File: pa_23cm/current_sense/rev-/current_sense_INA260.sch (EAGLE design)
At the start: 34 parts, among them IC1 INA260, IC2 MCP9700

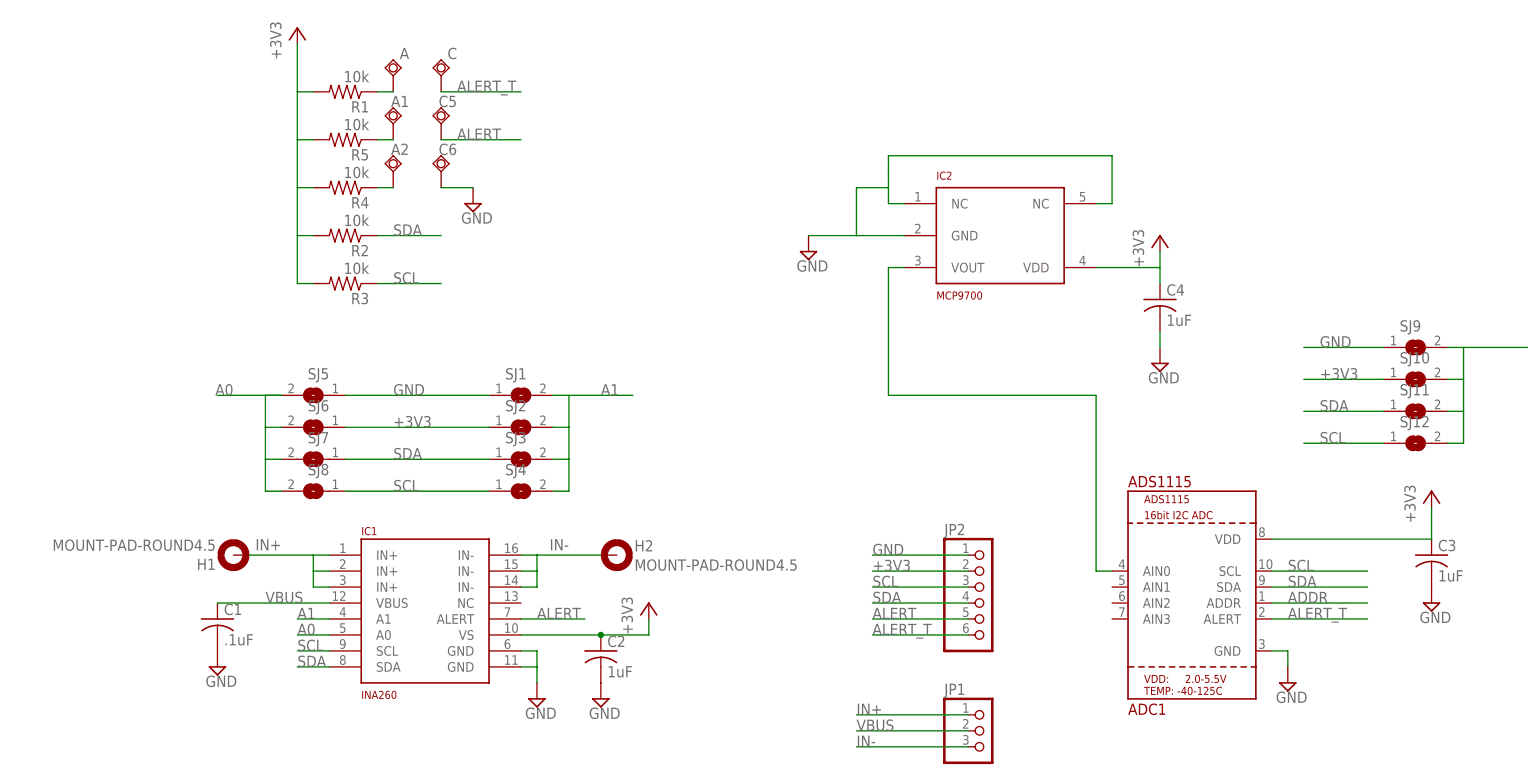
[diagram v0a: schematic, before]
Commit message: added Analog Input breakout for ADS1115 ADC.
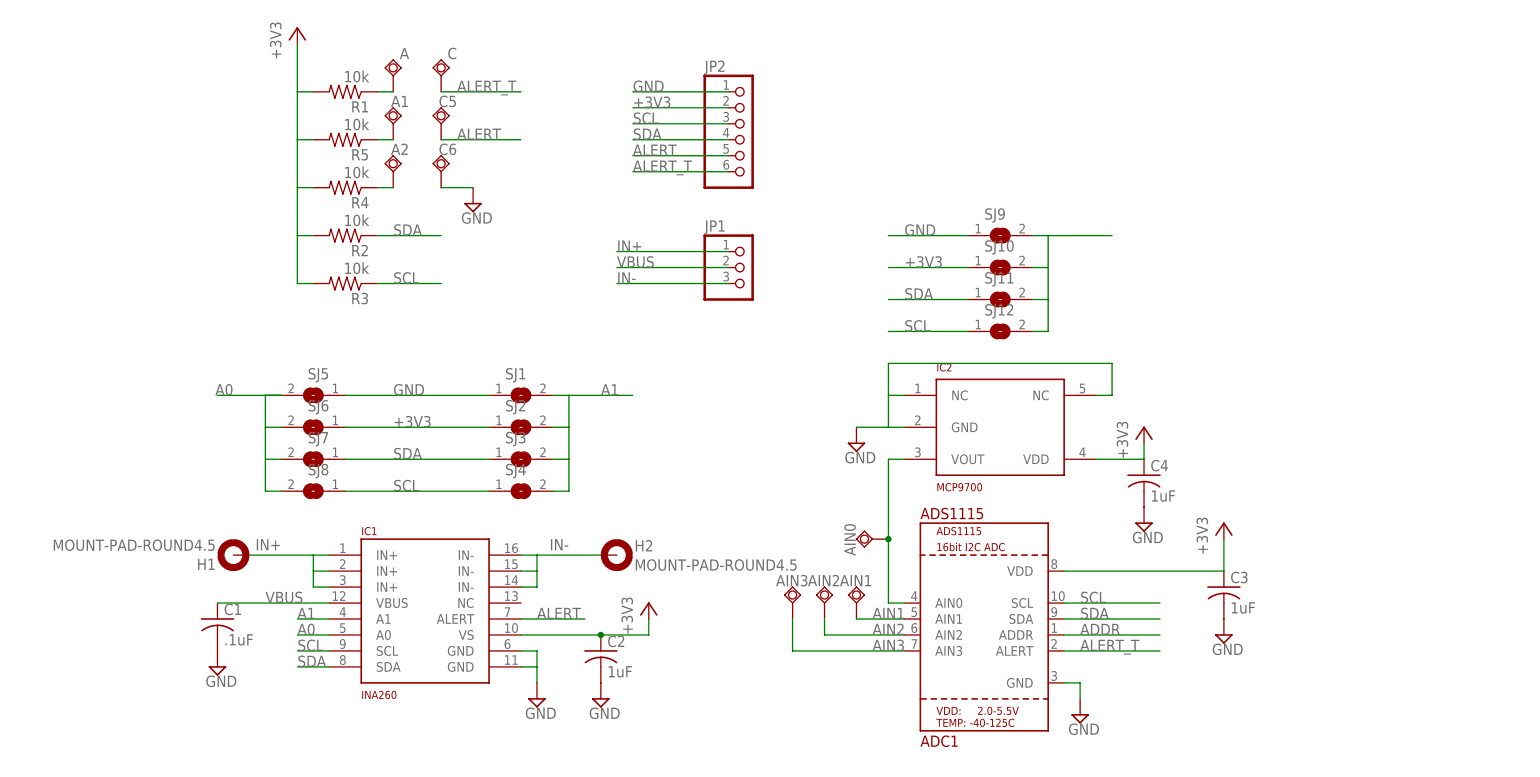
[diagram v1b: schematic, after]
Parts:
- added AIN0, AIN1, AIN2, AIN3: TPSQTP20SQ, testpad:TPSQTP20SQ
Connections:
- new net AIN1: ADC1.AIN1, AIN1.TP
- new net AIN2: ADC1.AIN2, AIN2.TP
- new net AIN3: ADC1.AIN3, AIN3.TP
- net V_TEMP: now also AIN0.TP
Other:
- moved on the sheet: ADC1, C3, C4, IC2, JP1, JP2, SJ10, SJ11, SJ12, SJ9
